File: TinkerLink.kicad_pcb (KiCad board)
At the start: 2 copper layers, 40 x 24 mm, 26 parts, among them J1 Conn_01x06_Pin, Q2 MMBT2222A, Q3 SQS411ENW-T1_GE3, Q4 SQS411ENW-T1_GE3, SW1 TS-061D-250D4-P, U1 ESP-01F-2M, U16 INA228, U3 AP63203WU

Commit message: ...
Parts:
- LOGO1: footprint LCSCfootprints:Creations logo med -> AUSTINfootprints:Creations logo med
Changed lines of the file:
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@@
 		(embedded_fonts no)
 	)
-	(footprint "LCSCfootprints:Creations logo med"
+	(footprint "AUSTINfootprints:Creations logo med"
 		(layer "B.Cu")
 		(at 104.3 95.6 180)

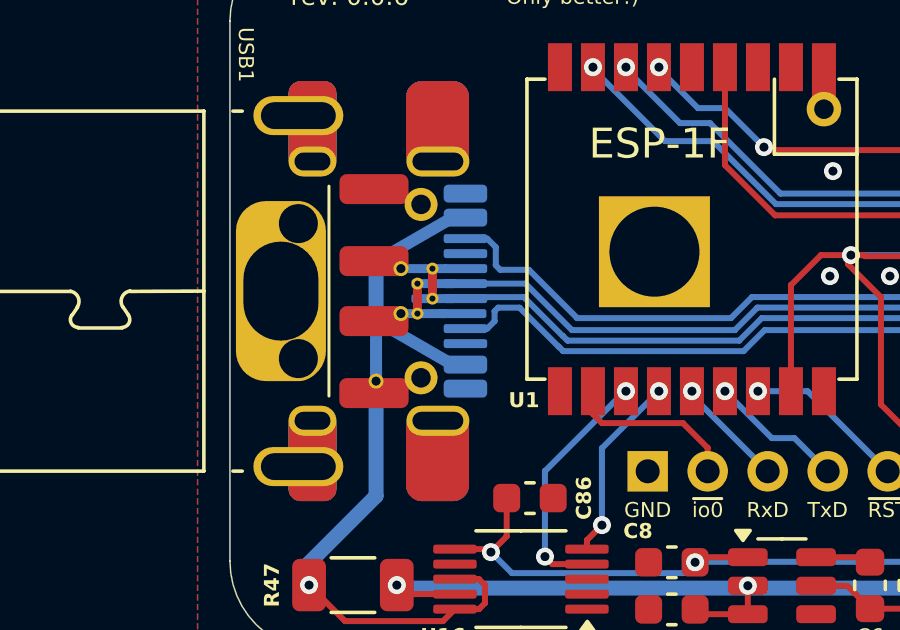
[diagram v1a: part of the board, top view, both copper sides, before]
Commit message: Added TPD2EUSB30A to D+/D- for ESD protection
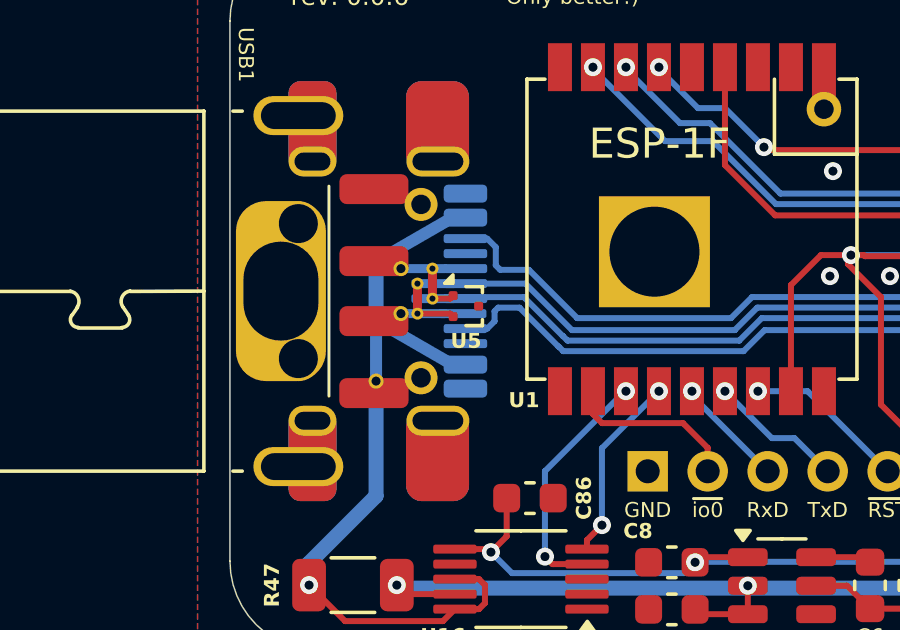
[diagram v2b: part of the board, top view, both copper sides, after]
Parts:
- added U5: TPD2EUSB30A, Package_TO_SOT_SMD:Texas_DRT-3, F.Cu at (87.9, 100.5)
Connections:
- net /D+ renamed D+
- net /D- renamed D-
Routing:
- net D-: track 25.3 -> 26.5 mm
- net D+: track 24.9 -> 25.6 mm

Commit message: Not twerks... tweaks!
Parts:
- moved R2 0.69 mm to (107.8, 108.1)
- moved REF** 0.55 mm to (107.9, 106.2), turned to 170 degrees
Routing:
- net Vdd: track 73.9 -> 67.9 mm
- net io14: track 10.2 -> 10.9 mm
- net D+: track 25.6 -> 26.3 mm
- net io12: track 28.4 -> 29.0 mm
- net /Tx: track 4.53 -> 5.12 mm
- net /RST: track 5.43 -> 5.99 mm
- net io13: track 39.3 -> 38.8 mm
- net GND: vias 3 -> 1

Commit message: can't... stop... tweakin'...
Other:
- board text added: "~{io13}"
- board text removed: "~{io4}"
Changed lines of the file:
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@@
 		(tags "capacitor")
 		(property "Reference" "C5"
-			(at 2.03 -0.99 0)
+			(at 0 -0.99 0)
 			(layer "F.SilkS")
 			(effects
@@
 			(effects
 				(font
-					(size 0.5 0.5)
-					(thickness 0.125)
+					(size 0.6 0.6)
+					(thickness 0.15)
+					(bold yes)
 				)
 			)
@@
 		(tags "capacitor")
 		(property "Reference" "C8"
-			(at 1.13 1.04 180)
+			(at 0 1.04 180)
 			(layer "F.SilkS")
 			(effects
@@
 		)
 	)
-	(gr_text "~{io4}"
-		(at 117.83 110.51 0)
+	(gr_text "~{io13}"
+		(at 117.66 110.51 0)
 		(layer "F.SilkS")
 		(effects

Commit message: ...
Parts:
- renumbered C86 to C1, R47 to R1, R1 to R2, R2 to R4, U16 to U2, U5 to U4
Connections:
- net Net-(U1-ANT) renamed Ant10a
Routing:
- net GND: vias 1 -> 0

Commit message: smaller AC logo
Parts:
- LOGO1: value Creations_logo_med -> Creations_logo_small; footprint AUSTINfootprints:Creations logo med -> AC_logos:Creations logo small
- moved LOGO1 3.11 mm to (107.4, 95.4)

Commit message: Nasty initial CC1/2 resistors solution
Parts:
- added R7: 5k1, Resistor_SMD:R_0603_1608Metric, F.Cu at (89.0, 103.0)
- added R8: 5k1, Resistor_SMD:R_0603_1608Metric, F.Cu at (89.0, 97.0)
- moved LOGO1 18.8 mm to (91.0, 104.6)
- moved U4 0.53 mm to (87.7, 100.0)
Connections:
- net CC renamed CC1
- net Vconn renamed CC2
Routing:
- net CC2: track 24.5 -> 25.4 mm, vias 0 -> 1
- net CC1: track 25.5 -> 25.8 mm, vias 0 -> 1
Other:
- board text added: "${COMPANY} 2026 ${COMMENT1}"
- board text removed: "${COMPANY} ${COMMENT1}"

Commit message: workin on some included libs...
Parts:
- LOGO1: footprint AC_logos:Creations logo small -> AUSTINfootprints:Creations logo small
- REF**: footprint tinker:DagNabbit -> TINKERfootprints:DagNabbit
